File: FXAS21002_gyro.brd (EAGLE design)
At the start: 15.2 x 15.2 mm, 9 parts

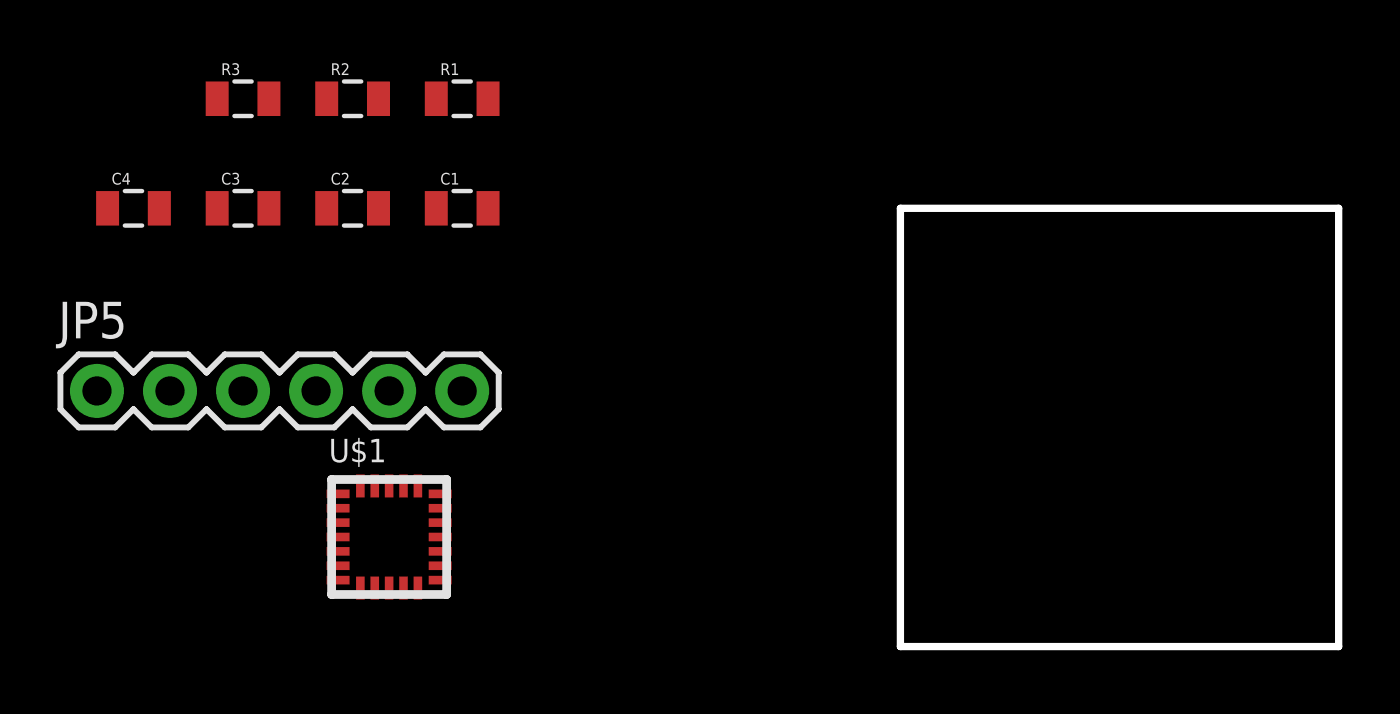
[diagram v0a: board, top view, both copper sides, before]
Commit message: all wires connected
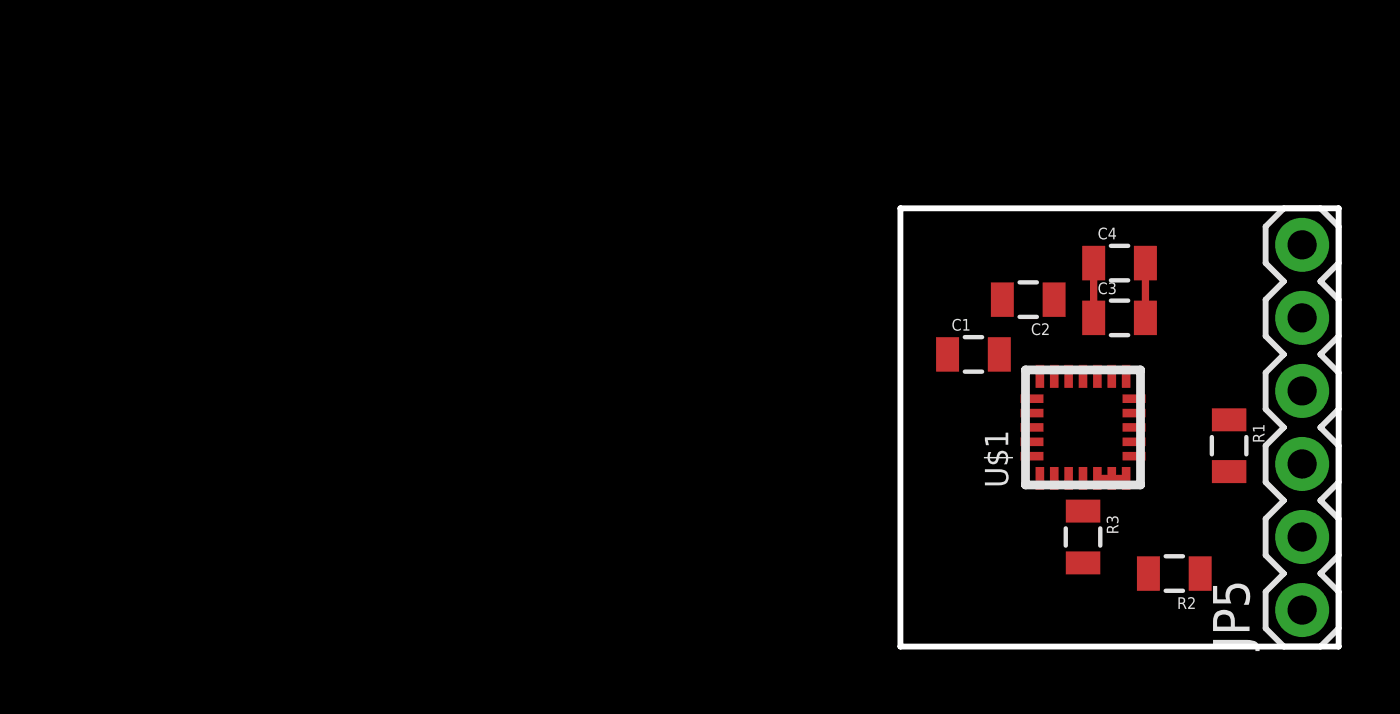
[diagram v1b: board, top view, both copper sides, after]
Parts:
- moved JP5 42.6 mm to (14.0, 1.27), turned to 90 degrees
- moved C4 34.3 mm to (7.62, 13.3)
- moved R2 33.0 mm to (9.53, 2.54), turned to 180 degrees
- moved R3 32.9 mm to (6.35, 3.81), turned to 270 degrees
- moved C3 30.7 mm to (7.62, 11.4)
- moved R1 29.3 mm to (11.4, 6.99), turned to 270 degrees
- moved U$1 24.4 mm to (6.35, 7.62), turned to 90 degrees
- moved C2 23.7 mm to (4.45, 12.1), turned to 180 degrees
- moved C1 18.5 mm to (2.54, 10.2)
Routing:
- net GND: track 0.00 -> 2.91 mm
- net +3V3: track 0.00 -> 1.91 mm
- added copper zone on layer 16, net GND
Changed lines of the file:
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@@
 <board>
 <plain>
-<wire x1="0" y1="0" x2="0" y2="15.24" width="0.254" layer="20"/>
-<wire x1="0" y1="15.24" x2="15.24" y2="15.24" width="0.254" layer="20"/>
-<wire x1="15.24" y1="15.24" x2="15.24" y2="0" width="0.254" layer="20"/>
-<wire x1="15.24" y1="0" x2="0" y2="0" width="0.254" layer="20"/>
+<wire x1="0" y1="0" x2="0" y2="15.24" width="0.2032" layer="20"/>
+<wire x1="0" y1="15.24" x2="15.24" y2="15.24" width="0.2032" layer="20"/>
+<wire x1="15.24" y1="15.24" x2="15.24" y2="0" width="0.2032" layer="20"/>
+<wire x1="15.24" y1="0" x2="0" y2="0" width="0.2032" layer="20"/>
 </plain>
 <attributes>
@@
 </autorouter>
 <elements>
-<element name="C1" library="SparkFun-Passives" package="0805" value="0.1uF" x="-15.24" y="15.24"/>
-<element name="C2" library="SparkFun-Passives" package="0805" value="100nF" x="-19.05" y="15.24"/>
-<element name="C3" library="SparkFun-Passives" package="0805" value="0.1uF" x="-22.86" y="15.24"/>
-<element name="C4" library="SparkFun-Passives" package="0805" value="1.0uF" x="-26.67" y="15.24"/>
-<element name="JP5" library="SparkFun" package="1X06" value="" x="-27.94" y="8.89"/>
-<element name="R1" library="SparkFun-Passives" package="0805" value="10k" x="-15.24" y="19.05"/>
-<element name="R2" library="SparkFun-Passives" package="0805" value="10k" x="-19.05" y="19.05"/>
-<element name="R3" library="SparkFun-Passives" package="0805" value="47k" x="-22.86" y="19.05"/>
-<element name="U$1" library="sharkdunio" package="24QFN" value="FXAS21002" x="-17.78" y="3.81"/>
+<element name="C1" library="SparkFun-Passives" package="0805" value="0.1uF" x="2.54" y="10.16"/>
+<element name="C2" library="SparkFun-Passives" package="0805" value="100nF" x="4.445" y="12.065" rot="R180"/>
+<element name="C3" library="SparkFun-Passives" package="0805" value="0.1uF" x="7.62" y="11.43"/>
+<element name="C4" library="SparkFun-Passives" package="0805" value="1.0uF" x="7.62" y="13.335"/>
+<element name="JP5" library="SparkFun" package="1X06" value="" x="13.97" y="1.27" rot="R90"/>
+<element name="R1" library="SparkFun-Passives" package="0805" value="10k" x="11.43" y="6.985" rot="R270"/>
+<element name="R2" library="SparkFun-Passives" package="0805" value="10k" x="9.525" y="2.54" rot="R180"/>
+<element name="R3" library="SparkFun-Passives" package="0805" value="47k" x="6.35" y="3.81" rot="R270"/>
+<element name="U$1" library="sharkdunio" package="24QFN" value="FXAS21002" x="6.35" y="7.62" rot="R90"/>
 </elements>
 <signals>
@@
 <contactref element="U$1" pad="1"/>
 <contactref element="JP5" pad="6"/>
-<wire x1="-19.555" y1="2.81" x2="-19.555" y2="2.31" width="0" layer="19" extent="1-1"/>
-<wire x1="-19.555" y1="3.31" x2="-19.555" y2="2.81" width="0" layer="19" extent="1-1"/>
-<wire x1="-18.78" y1="2.035" x2="-19.555" y2="2.31" width="0" layer="19" extent="1-1"/>
-<wire x1="-18.28" y1="2.035" x2="-18.78" y2="2.035" width="0" layer="19" extent="1-1"/>
-<wire x1="-17.78" y1="2.035" x2="-18.28" y2="2.035" width="0" layer="19" extent="1-1"/>
-<wire x1="-16.005" y1="2.31" x2="-17.78" y2="2.035" width="0" layer="19" extent="1-1"/>
-<wire x1="-16.005" y1="2.81" x2="-16.005" y2="2.31" width="0" layer="19" extent="1-1"/>
-<wire x1="-19.555" y1="5.31" x2="-19.555" y2="3.31" width="0" layer="19" extent="1-1"/>
-<wire x1="-18.78" y1="5.585" x2="-19.555" y2="5.31" width="0" layer="19" extent="1-1"/>
-<wire x1="-18.28" y1="5.585" x2="-18.78" y2="5.585" width="0" layer="19" extent="1-1"/>
-<wire x1="-17.78" y1="5.585" x2="-18.28" y2="5.585" width="0" layer="19" extent="1-1"/>
-<wire x1="-17.28" y1="5.585" x2="-17.78" y2="5.585" width="0" layer="19" extent="1-1"/>
-<wire x1="-16.78" y1="5.585" x2="-17.28" y2="5.585" width="0" layer="19" extent="1-1"/>
-<wire x1="-16.005" y1="5.31" x2="-16.78" y2="5.585" width="0" layer="19" extent="1-1"/>
-<wire x1="-15.24" y1="8.89" x2="-16.78" y2="5.585" width="0" layer="19" extent="1-1"/>
-<wire x1="-16.14" y1="15.24" x2="-15.24" y2="8.89" width="0" layer="19" extent="1-1"/>
-<wire x1="-18.15" y1="15.24" x2="-16.14" y2="15.24" width="0" layer="19" extent="1-1"/>
-<wire x1="-21.96" y1="15.24" x2="-18.15" y2="15.24" width="0" layer="19" extent="1-1"/>
-<wire x1="-25.77" y1="15.24" x2="-21.96" y2="15.24" width="0" layer="19" extent="1-1"/>
+<polygon width="0.254" layer="16" isolate="0.3048">
+<vertex x="0" y="15.24"/>
+<vertex x="15.24" y="15.24"/>
+<vertex x="15.24" y="0"/>
+<vertex x="0" y="0"/>
+</polygon>
+<wire x1="8.52" y1="11.43" x2="8.52" y2="13.335" width="0.254" layer="1"/>
+<wire x1="6.85" y1="5.845" x2="7.35" y2="5.845" width="0.254" layer="1"/>
+<wire x1="7.35" y1="5.845" x2="7.85" y2="5.845" width="0.254" layer="1"/>
+<wire x1="7.85" y1="9.395" x2="8.52" y2="11.43" width="0" layer="19" extent="1-1"/>
+<wire x1="7.35" y1="9.395" x2="7.85" y2="9.395" width="0" layer="19" extent="1-1"/>
+<wire x1="8.125" y1="7.62" x2="7.85" y2="9.395" width="0" layer="19" extent="1-1"/>
+<wire x1="8.125" y1="7.12" x2="8.125" y2="7.62" width="0" layer="19" extent="1-1"/>
+<wire x1="8.125" y1="6.62" x2="8.125" y2="7.12" width="0" layer="19" extent="1-1"/>
+<wire x1="7.85" y1="5.845" x2="8.125" y2="6.62" width="0" layer="19" extent="1-1"/>
+<wire x1="4.85" y1="5.845" x2="6.85" y2="5.845" width="0" layer="19" extent="1-1"/>
+<wire x1="4.575" y1="6.62" x2="4.85" y2="5.845" width="0" layer="19" extent="1-1"/>
+<wire x1="4.575" y1="7.12" x2="4.575" y2="6.62" width="0" layer="19" extent="1-1"/>
+<wire x1="4.575" y1="7.62" x2="4.575" y2="7.12" width="0" layer="19" extent="1-1"/>
+<wire x1="4.575" y1="8.12" x2="4.575" y2="7.62" width="0" layer="19" extent="1-1"/>
+<wire x1="4.575" y1="8.62" x2="4.575" y2="8.12" width="0" layer="19" extent="1-1"/>
+<wire x1="4.85" y1="9.395" x2="4.575" y2="8.62" width="0" layer="19" extent="1-1"/>
+<wire x1="3.545" y1="12.065" x2="4.85" y2="9.395" width="0" layer="19" extent="1-1"/>
+<wire x1="1.64" y1="10.16" x2="3.545" y2="12.065" width="0" layer="19" extent="1-1"/>
+<wire x1="13.97" y1="13.97" x2="8.52" y2="13.335" width="0" layer="19" extent="1-1"/>
 </signal>
 <signal name="SCL">
@@
 <contactref element="R1" pad="1"/>
 <contactref element="JP5" pad="3"/>
-<wire x1="-22.86" y1="8.89" x2="-17.28" y2="2.035" width="0" layer="19" extent="1-1"/>
-<wire x1="-16.14" y1="19.05" x2="-22.86" y2="8.89" width="0" layer="19" extent="1-1"/>
+<wire x1="13.97" y1="6.35" x2="11.43" y2="7.885" width="0" layer="19" extent="1-1"/>
+<wire x1="8.125" y1="8.12" x2="11.43" y2="7.885" width="0" layer="19" extent="1-1"/>
 </signal>
 <signal name="SDA">
@@
 <contactref element="R2" pad="2"/>
 <contactref element="JP5" pad="2"/>
-<wire x1="-16.78" y1="2.035" x2="-25.4" y2="8.89" width="0" layer="19" extent="1-1"/>
-<wire x1="-18.15" y1="19.05" x2="-25.4" y2="8.89" width="0" layer="19" extent="1-1"/>
+<wire x1="8.625" y1="2.54" x2="8.125" y2="8.62" width="0" layer="19" extent="1-1"/>
+<wire x1="13.97" y1="3.81" x2="8.625" y2="2.54" width="0" layer="19" extent="1-1"/>
 </signal>
 <signal name="+3V3">
@@
 <contactref element="R3" pad="2"/>
 <contactref element="JP5" pad="1"/>
-<wire x1="-27.57" y1="15.24" x2="-27.94" y2="8.89" width="0" layer="19" extent="1-1"/>
-<wire x1="-23.76" y1="15.24" x2="-27.57" y2="15.24" width="0" layer="19" extent="1-1"/>
-<wire x1="-21.96" y1="19.05" x2="-23.76" y2="15.24" width="0" layer="19" extent="1-1"/>
-<wire x1="-19.95" y1="19.05" x2="-21.96" y2="19.05" width="0" layer="19" extent="1-1"/>
-<wire x1="-14.34" y1="19.05" x2="-19.95" y2="19.05" width="0" layer="19" extent="1-1"/>
-<wire x1="-14.34" y1="15.24" x2="-14.34" y2="19.05" width="0" layer="19" extent="1-1"/>
-<wire x1="-16.005" y1="4.81" x2="-14.34" y2="15.24" width="0" layer="19" extent="1-1"/>
-<wire x1="-16.005" y1="4.31" x2="-16.005" y2="4.81" width="0" layer="19" extent="1-1"/>
-<wire x1="-16.005" y1="3.31" x2="-16.005" y2="4.31" width="0" layer="19" extent="1-1"/>
+<wire x1="6.72" y1="13.335" x2="6.72" y2="11.43" width="0.254" layer="1"/>
+<wire x1="10.425" y1="2.54" x2="11.43" y2="6.085" width="0" layer="19" extent="1-1"/>
+<wire x1="13.97" y1="1.27" x2="10.425" y2="2.54" width="0" layer="19" extent="1-1"/>
+<wire x1="6.35" y1="2.91" x2="10.425" y2="2.54" width="0" layer="19" extent="1-1"/>
+<wire x1="6.85" y1="9.395" x2="11.43" y2="6.085" width="0" layer="19" extent="1-1"/>
+<wire x1="5.85" y1="9.395" x2="6.85" y2="9.395" width="0" layer="19" extent="1-1"/>
+<wire x1="5.35" y1="9.395" x2="5.85" y2="9.395" width="0" layer="19" extent="1-1"/>
+<wire x1="6.72" y1="11.43" x2="6.85" y2="9.395" width="0" layer="19" extent="1-1"/>
+<wire x1="3.44" y1="10.16" x2="5.35" y2="9.395" width="0" layer="19" extent="1-1"/>
 </signal>
 <signal name="N$1">
 <contactref element="U$1" pad="16"/>
 <contactref element="C2" pad="1"/>
-<wire x1="-19.95" y1="15.24" x2="-16.005" y2="3.81" width="0" layer="19" extent="1-1"/>
+<wire x1="6.35" y1="9.395" x2="5.345" y2="12.065" width="0" layer="19" extent="1-1"/>
 </signal>
 <signal name="N$4">
 <contactref element="U$1" pad="4"/>
 <contactref element="R3" pad="1"/>
-<wire x1="-23.76" y1="19.05" x2="-19.555" y2="3.81" width="0" layer="19" extent="1-1"/>
+<wire x1="6.35" y1="4.71" x2="6.35" y2="5.845" width="0" layer="19" extent="1-1"/>
 </signal>
 <signal name="INT2">
 <contactref element="U$1" pad="2"/>
 <contactref element="JP5" pad="5"/>
-<wire x1="-17.78" y1="8.89" x2="-19.555" y2="4.81" width="0" layer="19" extent="1-1"/>
+<wire x1="5.35" y1="5.845" x2="13.97" y2="11.43" width="0" layer="19" extent="1-1"/>
 </signal>
 </signals>

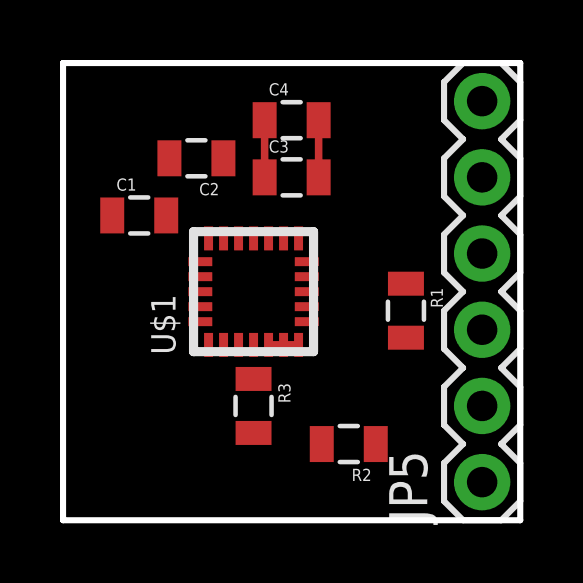
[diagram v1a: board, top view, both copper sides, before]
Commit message: changed int2 pin
did this to shorten trace to int2
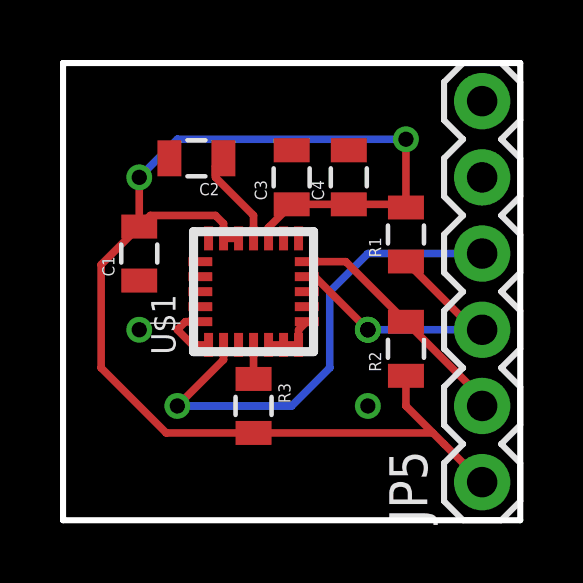
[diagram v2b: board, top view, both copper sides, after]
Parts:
- moved R2 3.70 mm to (11.4, 5.71), turned to 90 degrees
- moved C4 2.69 mm to (9.53, 11.4), turned to 90 degrees
- moved R1 2.54 mm to (11.4, 9.53), turned to 90 degrees
- moved C1 1.27 mm to (2.54, 8.89), turned to 90 degrees
- turned C3 to 90 degrees
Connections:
- net INT2: now also JP5.4; no longer JP5.5
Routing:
- net +3V3: track 1.91 -> 44.5 mm, vias 0 -> 2
- net INT2: track 0.00 -> 16.4 mm, vias 0 -> 1
- net SCL: track 0.00 -> 10.1 mm, vias 0 -> 1
- net SDA: track 0.00 -> 7.99 mm
- net N$1: track 0.00 -> 3.31 mm
- net N$4: track 0.00 -> 1.13 mm
- net GND: track 2.91 -> 4.01 mm, vias 0 -> 2
- added copper zone on layer 1, net GND
